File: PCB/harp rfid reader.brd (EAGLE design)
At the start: 37.5 x 26.5 mm, 38 parts, among them IC1 FT232RL, IC2 LP5907MFX-3.3, IC3 ATXMEGAxxxA4U-AU, Q1 BC817-40W, U1 ID-12/20SMD

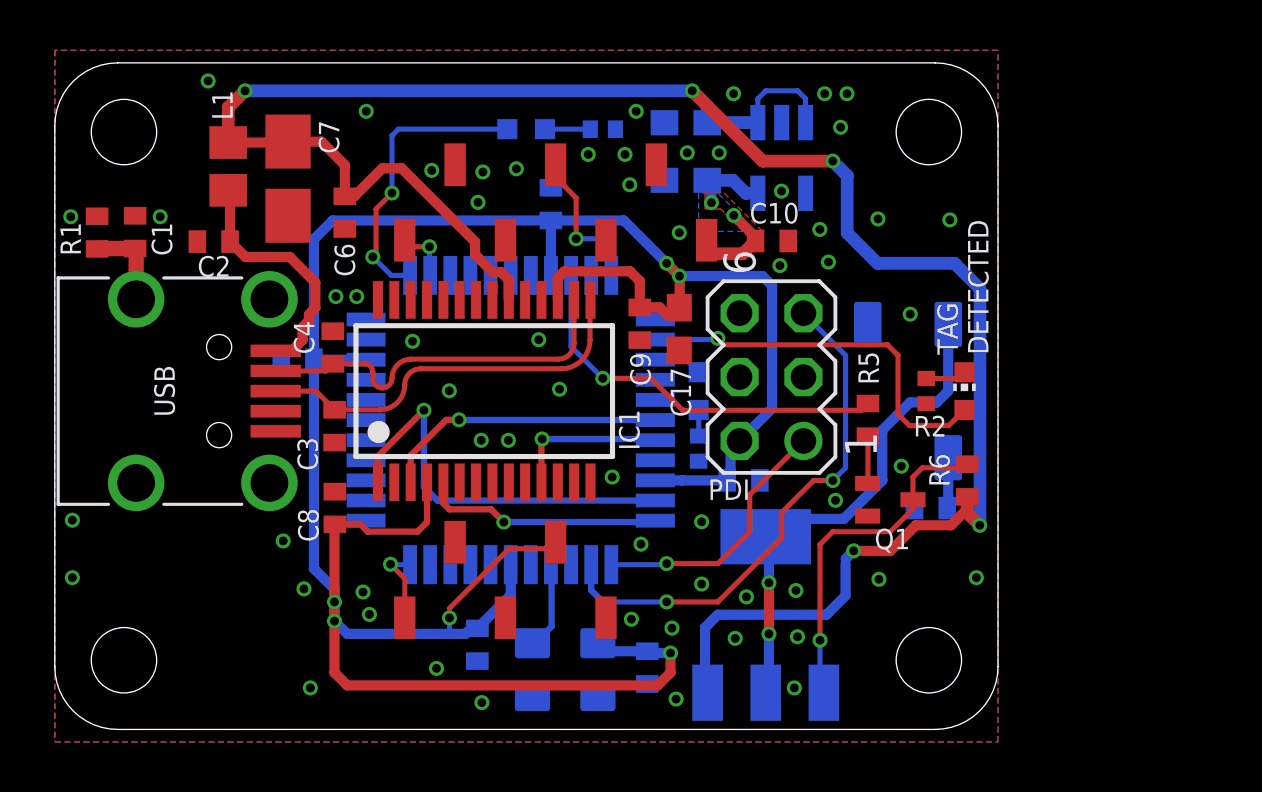
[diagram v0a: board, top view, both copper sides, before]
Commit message: Added 3 new capacitors.
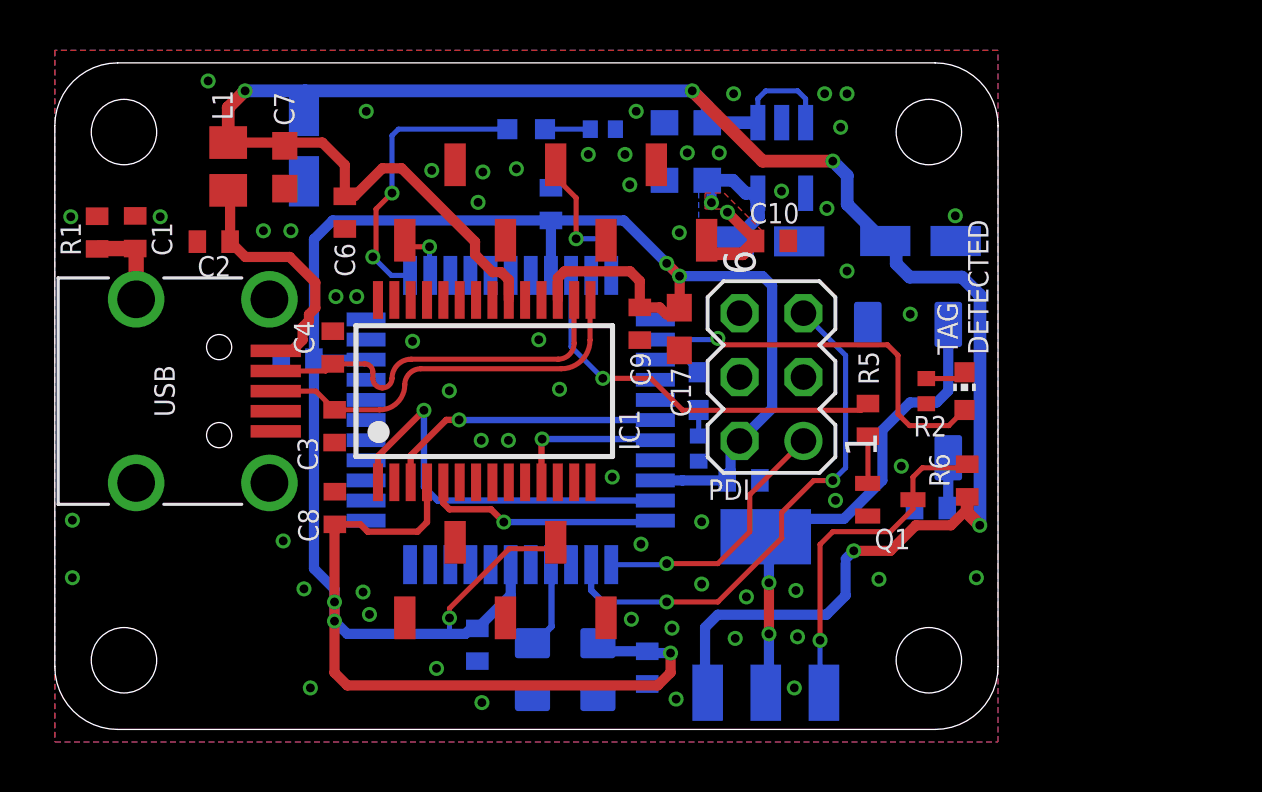
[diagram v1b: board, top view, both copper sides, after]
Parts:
- added C18, C19, C20: 100uF, rcl:CT3216
- C7: value 4.7uF -> 10uF; device rcl:A/3216-18W -> rcl:C0603
- moved C7 0.48 mm to (9.14, 22.4), turned to 270 degrees
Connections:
- removed net F1: IC3.44, U1.5
- net +5V: now also C19.+, C20.+, C7.1; no longer C7.+
- net GND: now also C18.-, C19.-, C20.-, C7.2; no longer C7.-
- net N$1: now also C18.+
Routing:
- net F1: track 3.15 -> 0.00 mm, vias 1 -> 0
- net N$1: track 7.25 -> 10.0 mm
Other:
- board text added: "+"
- board text added: "harp RFID reader v1.1"
- board text removed: "harp RFID reader v1.0"

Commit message: Corrected STATE and DETECT lines and increased LED resistors.
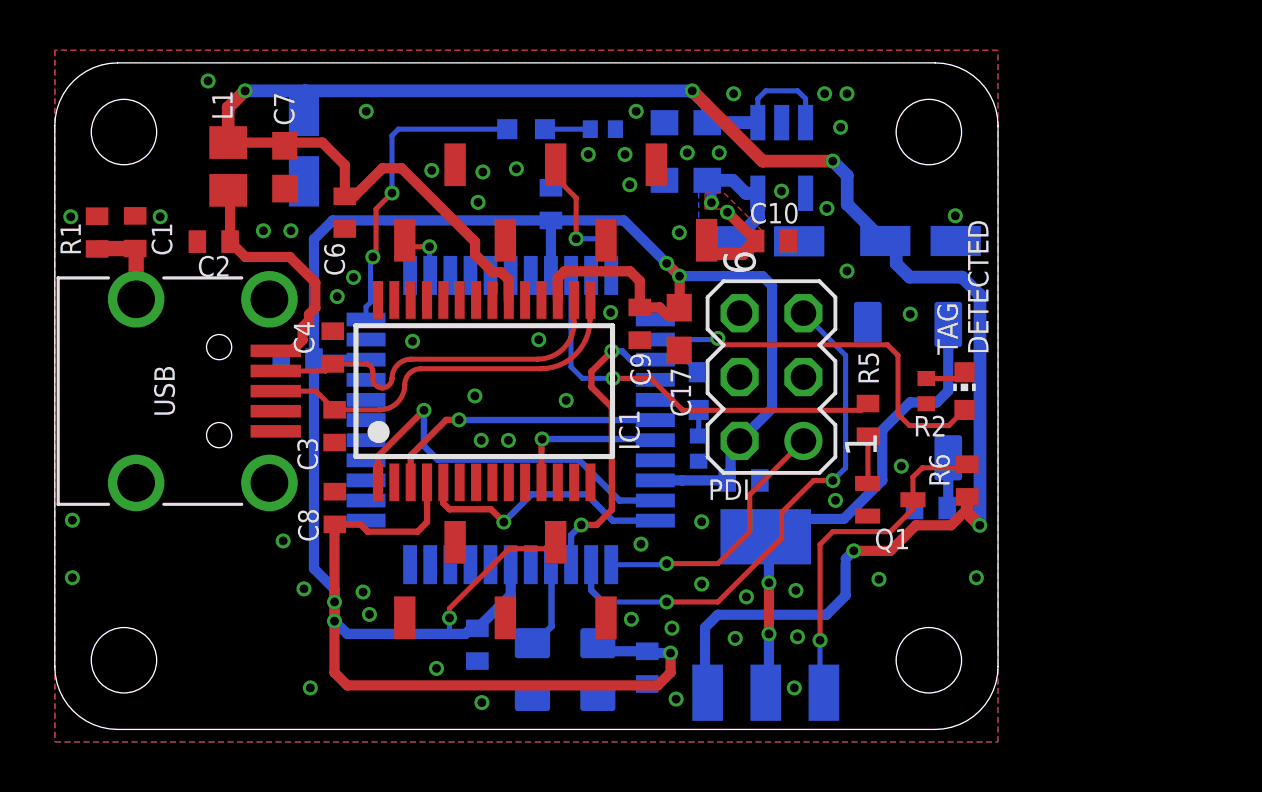
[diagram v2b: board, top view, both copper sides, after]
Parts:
- IC3: value ATXMEGAxxxA4U-AU -> ATXMEGA32A4U-AU
- R2, R3, R4: value 910 -> 1k
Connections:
- net DETECT1: now also IC3.11; no longer IC3.12
- net STATE: now also IC3.36
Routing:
- net STATE: track 1.93 -> 14.1 mm, vias 0 -> 2
- net FT_TXD: track 16.1 -> 15.1 mm
- net FT_RXD: track 9.59 -> 10.5 mm
- net DETECT1: track 11.6 -> 12.4 mm
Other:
- board text added: "harp RFID reader v1.2"
- board text removed: "harp RFID reader v1.1"

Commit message: Added a digital output.
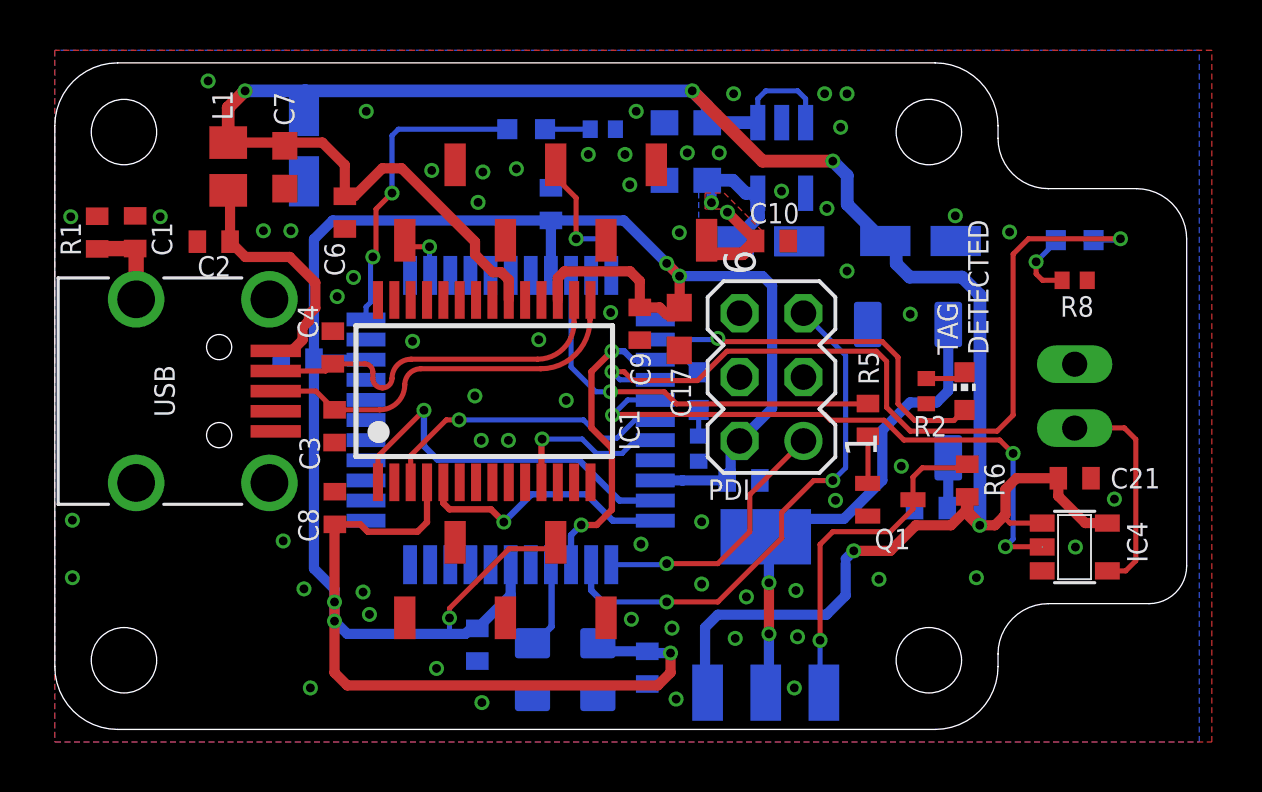
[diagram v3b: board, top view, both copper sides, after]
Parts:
- added C21: 100nF, rcl:C0402
- added IC4: (no value), 74xx-little-de:SOT23-5
- added OUT: 22-23-2021, con-molex:22-23-2021
- added OUT0: (no value), led:CHIP-LED0603
- added R8: 1k, rcl:R0402
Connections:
- new net N$6: OUT0.C, R8.2
- new net N$7: IC4.4, OUT.1
- new net OUT0: IC3.27, IC4.2
- new net OUT0_LED: IC3.26, OUT0.A
- net +5V: now also C21.1, IC4.1, IC4.5
- net GND: now also C21.2, IC4.3, OUT.2, R8.1
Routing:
- net OUT0_LED: track 0.00 -> 33.1 mm, vias 0 -> 2
- net OUT0: track 0.00 -> 23.8 mm, vias 0 -> 3
- net +5V: track 87.4 -> 96.7 mm
- net N$7: track 0.00 -> 8.75 mm
- net N$6: track 0.00 -> 2.80 mm, vias 0 -> 1
- net FT_RTS: track 11.4 -> 12.0 mm
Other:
- board size 37.5 x 26.5 mm -> 45 x 26.5 mm
- board text added: "G"
- board text added: "OUT0"
- board text removed: "GND"
- board text removed: "VCC"
- board text removed: "clk"
- board text removed: "data"
